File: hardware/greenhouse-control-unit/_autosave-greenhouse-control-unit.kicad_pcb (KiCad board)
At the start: 2 copper layers, 150 x 90 mm, 50 parts, among them J1 Buck_Conn_01x01_Female, J10 Conn_01x08, J11 Conn_01x08, J12 Conn_01x05_Female, J13 Molex_KK-396_01x08, J14 Molex_KK-254_01x05, J15 Conn_01x05_Female, J16 Conn_01x05_Female, J17 Molex_KK-254_01x04, J2 Buck_Conn_01x01_Female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

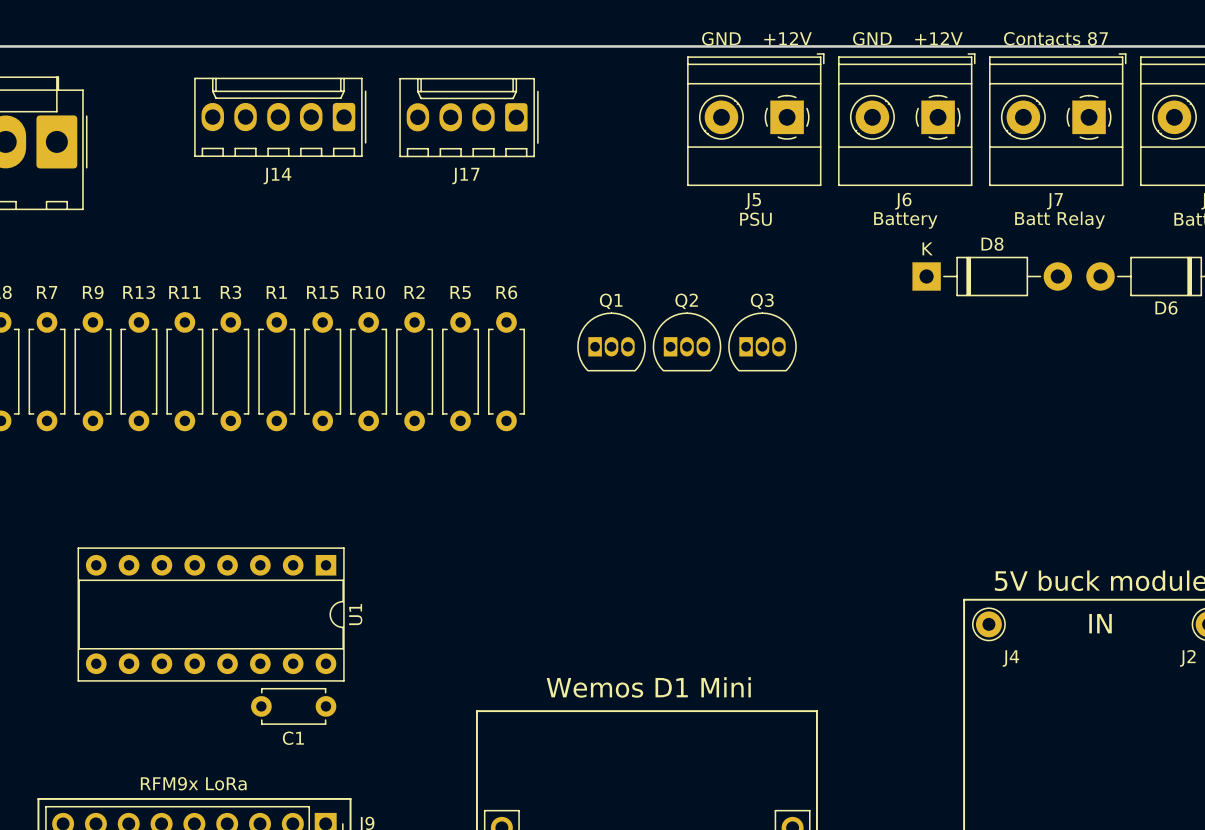
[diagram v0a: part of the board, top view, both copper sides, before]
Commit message: Replace relay with sink FET
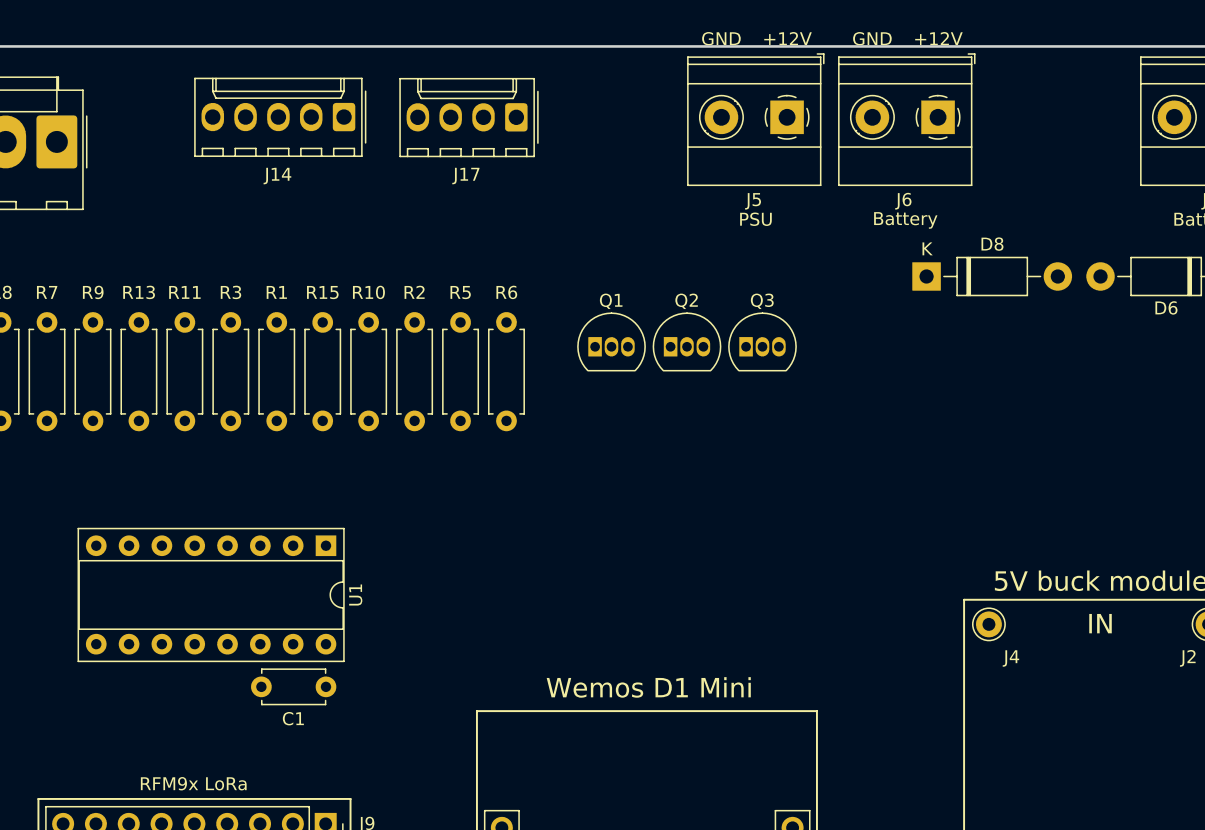
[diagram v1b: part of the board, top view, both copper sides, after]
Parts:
- removed J7: Pluggable_Terminal_01x02, TerminalBlock_Phoenix:TerminalBlock_Phoenix_MKDS-1,5-2-5.08_1x02_P5.08mm_Horizontal
- moved C1 1.51 mm to (103.4, 114.6)
- moved U1 1.51 mm to (103.4, 103.6)
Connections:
- J6 pad 1: /Batt+10V -> +10V
